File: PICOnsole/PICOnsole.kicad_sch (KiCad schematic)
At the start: 32 parts, among them J1 UART Headers, J2 Vibration Motor, J3 Amp Gain Jumper, J4 Amp Gain Jumper2, SW1 A Button, SW10 Power Switch, SW2 X Button, SW3 Start Button, SW4 B Button, SW5 Y Button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

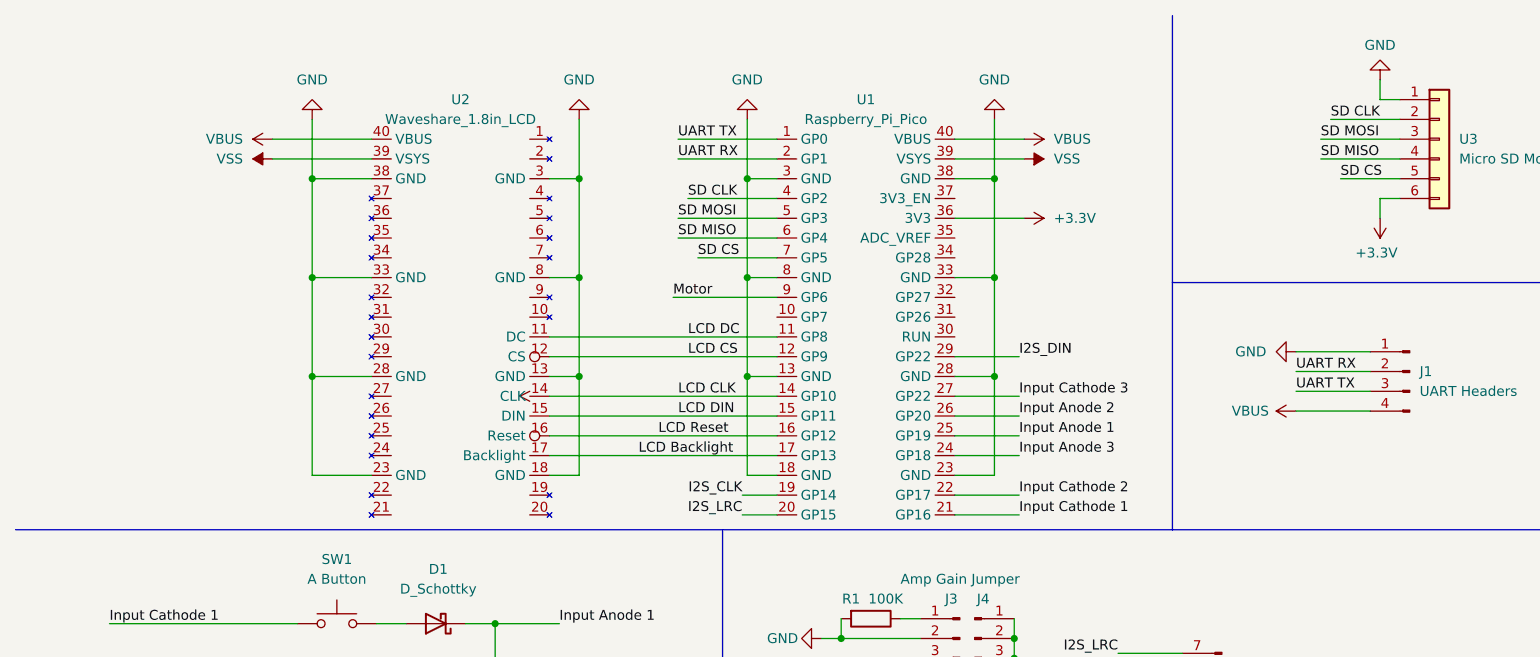
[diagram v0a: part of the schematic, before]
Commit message: Increased OS RAM size to allow for better errors. Currently programs can't find builtin functions (eg memset) correctly
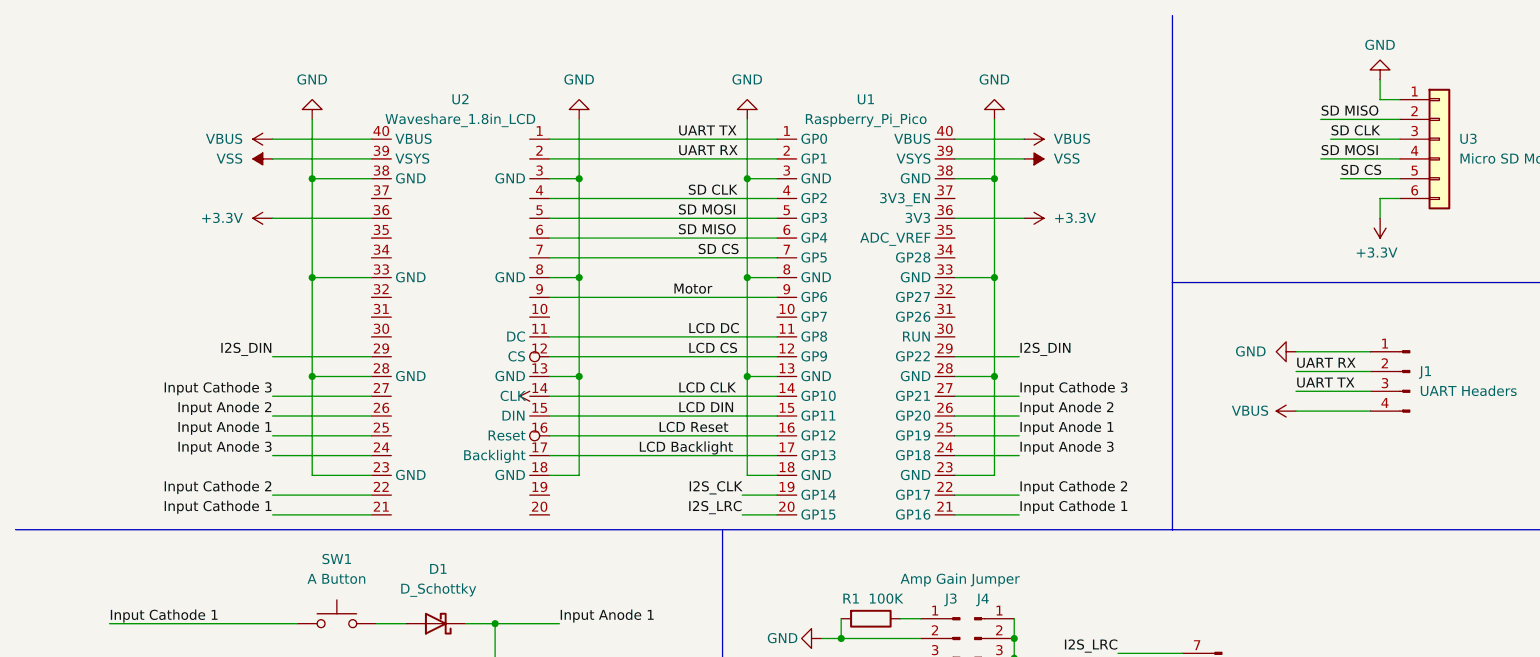
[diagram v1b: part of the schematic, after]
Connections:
- net +3V3: now also U2.36
- net I2S_DIN: now also U2.29
- net Input Anode 1: now also U2.25
- net Input Anode 2: now also U2.26
- net Input Anode 3: now also U2.24
- net Input Cathode 1: now also U2.21
- net Input Cathode 2: now also U2.22
- net Input Cathode 3: now also U2.27
- net Motor: now also U2.9
- net SD CLK: now also U2.4, U3.3 (Pin_3); no longer U3.2 (Pin_2)
- net SD CS: now also U2.7
- net SD MISO: now also U2.6, U3.2 (Pin_2); no longer U3.4 (Pin_4)
- net SD MOSI: now also U2.5, U3.4 (Pin_4); no longer U3.3 (Pin_3)
- net UART RX: now also U2.2
- net UART TX: now also U2.1
